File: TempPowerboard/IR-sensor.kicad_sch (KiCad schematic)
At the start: 28 parts, among them IC6 ADC122S051CIMMX_NOPB, J10 Dribbler Temp, J11 Kicker, J7 IR1, J9 IR2, Q7 BSS138, Q8 PMOS

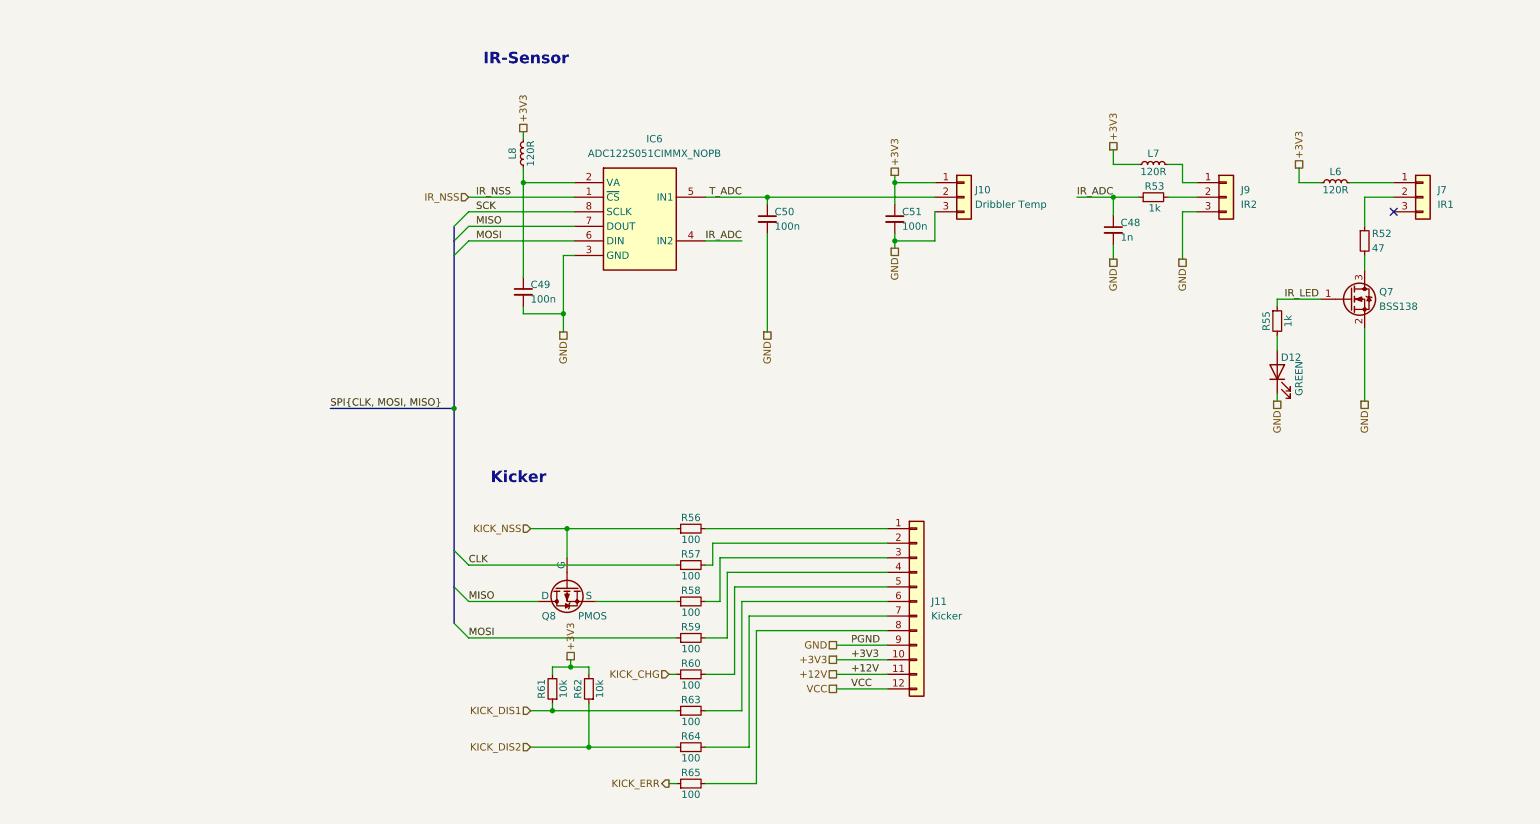
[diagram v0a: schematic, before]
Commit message: Devboard ports defined
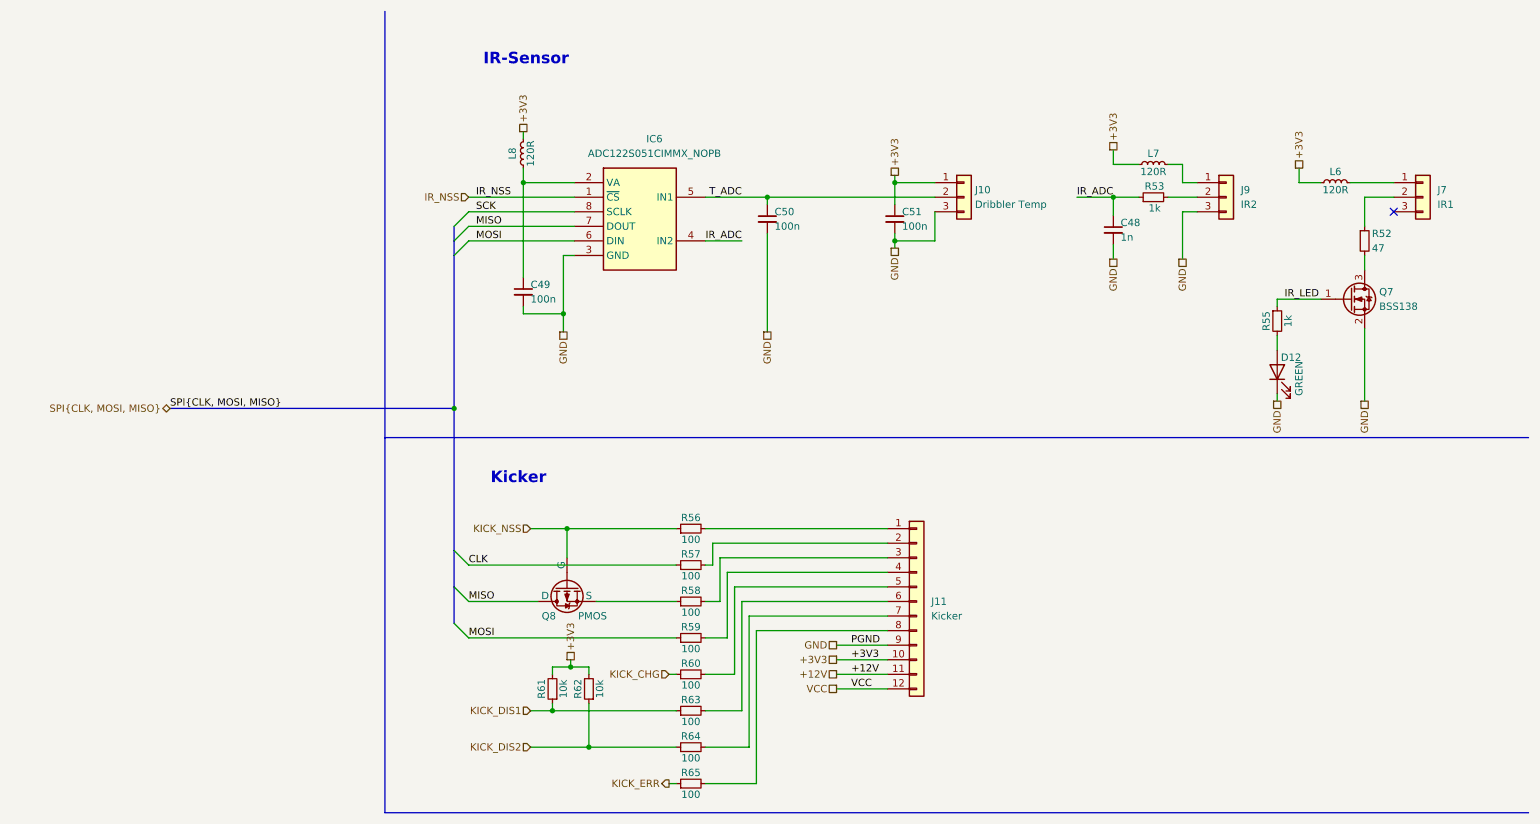
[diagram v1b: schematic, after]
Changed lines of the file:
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@@
   (junction (at 118.11 126.365) (diameter 0) (color 0 0 0 0)
   )
+  (junction (at 97.79 81.28) (diameter 0) (color 0 0 0 0)
+  )
   (junction (at 114.935 133.985) (diameter 0) (color 0 0 0 0)
   )
@@
   )
   (junction (at 121.285 140.335) (diameter 0) (color 0 0 0 0)
-  )
-  (junction (at 97.79 81.28) (diameter 0) (color 0 0 0 0)
   )
   (no_connect (at 261.62 46.99))
@@
     (stroke (width 0) (type default))
   )
+  (bus (pts (xy 97.79 81.28) (xy 97.79 106.045))
+    (stroke (width 0) (type default))
+  )
+  (polyline (pts (xy 85.725 12.065) (xy 85.725 86.36))
+    (stroke (width 0) (type default))
+  )
   (wire (pts (xy 142.875 108.585) (xy 142.875 104.775))
     (stroke (width 0) (type default))
@@
     (stroke (width 0) (type default))
   )
+  (polyline (pts (xy 85.725 151.765) (xy 285.115 151.765))
+    (stroke (width 0) (type default))
+  )
   (wire (pts (xy 122.555 114.935) (xy 136.525 114.935))
     (stroke (width 0) (type default))
@@
     (stroke (width 0) (type default))
   )
-  (bus (pts (xy 97.79 81.28) (xy 97.79 106.045))
-    (stroke (width 0) (type default))
-  )
   (wire (pts (xy 164.465 127.635) (xy 173.355 127.635))
     (stroke (width 0) (type default))
@@
     (stroke (width 0) (type default))
   )
+  (polyline (pts (xy 85.725 86.36) (xy 85.725 151.765))
+    (stroke (width 0) (type default))
+  )
   (bus (pts (xy 97.79 106.045) (xy 97.79 112.395))
     (stroke (width 0) (type default))
@@
     (stroke (width 0) (type default))
   )
+  (polyline (pts (xy 85.725 86.36) (xy 285.115 86.36))
+    (stroke (width 0) (type default))
+  )
   (wire (pts (xy 150.495 120.015) (xy 173.355 120.015))
     (stroke (width 0) (type default))
@@
     (stroke (width 0) (type default))
   )
-  (bus (pts (xy 76.2 81.28) (xy 97.79 81.28))
+  (bus (pts (xy 48.26 81.28) (xy 97.79 81.28))
     (stroke (width 0) (type default))
   )
@@
     (effects (font (size 1.27 1.27)) (justify left bottom))
   )
-  (label "SPI{CLK, MOSI, MISO}" (at 76.2 81.28 0) (fields_autoplaced)
+  (label "SPI{CLK, MOSI, MISO}" (at 48.26 81.28 0) (fields_autoplaced)
     (effects (font (size 1.27 1.27)) (justify left bottom))
   )
@@
     (effects (font (size 1.27 1.27)) (justify right))
   )
+  (hierarchical_label "SPI{CLK, MOSI, MISO}" (shape bidirectional) (at 48.26 81.28 180) (fields_autoplaced)
+    (effects (font (size 1.27 1.27)) (justify right))
+  )
